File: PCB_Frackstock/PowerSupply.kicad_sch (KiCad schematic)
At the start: 25 parts, among them J2 105450-0101, U12 SPX3819M5-L-3-3, U13 SGM6603-5.0YN6G_TR, U14 1043, U3 MCP73871-2CC

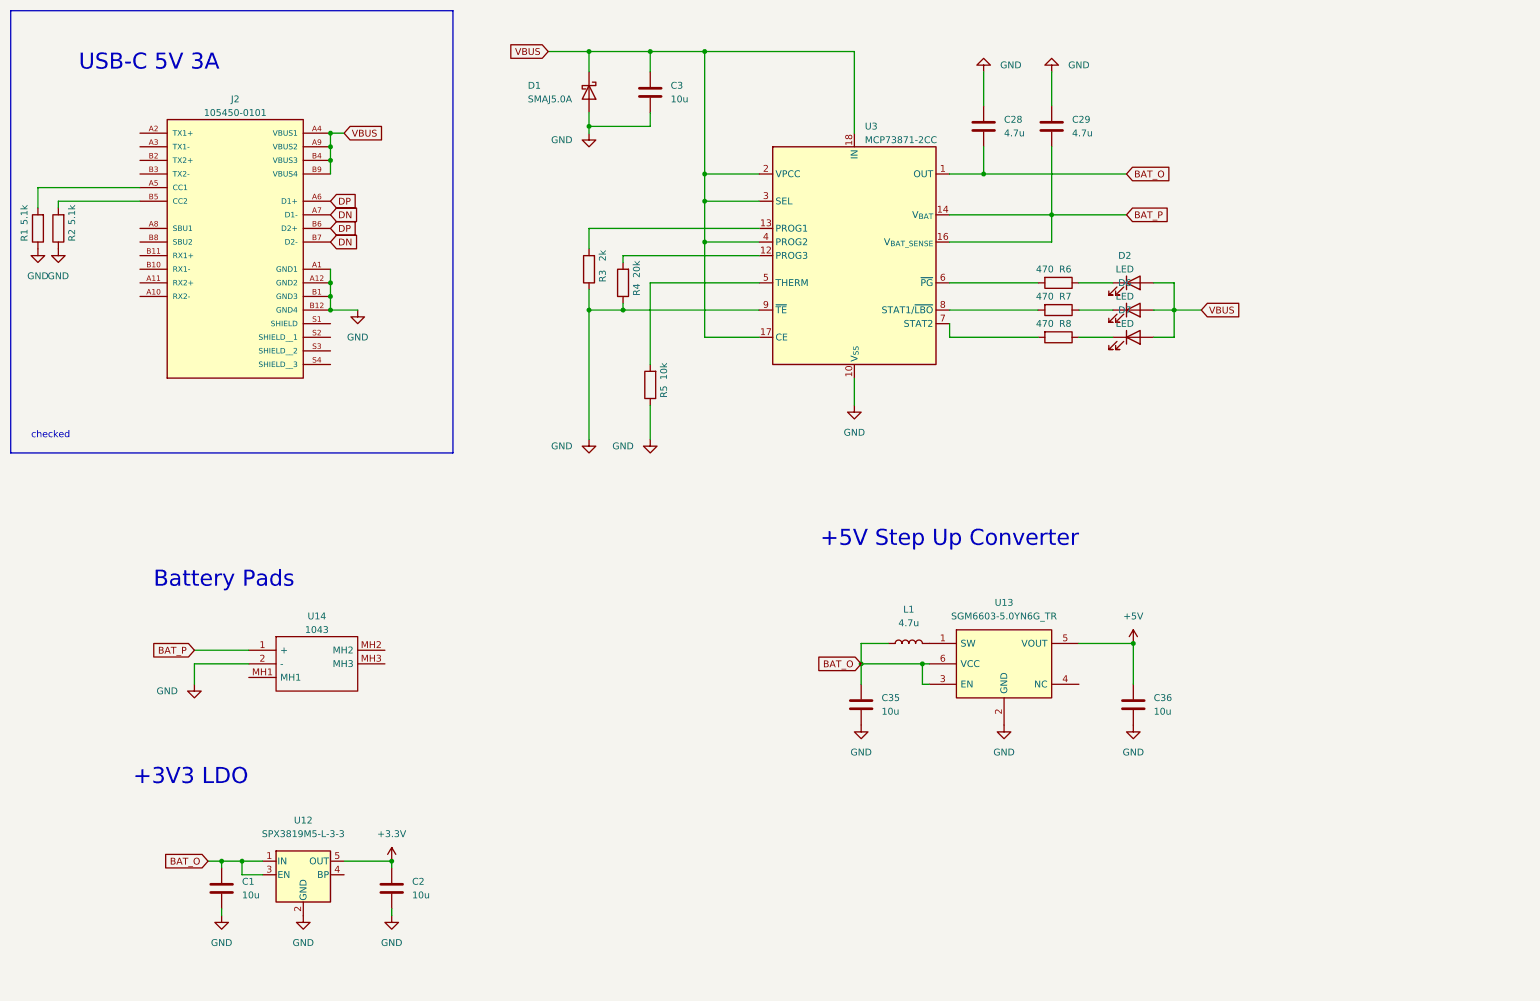
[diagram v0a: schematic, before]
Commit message: Battery Management and change parts to 0603
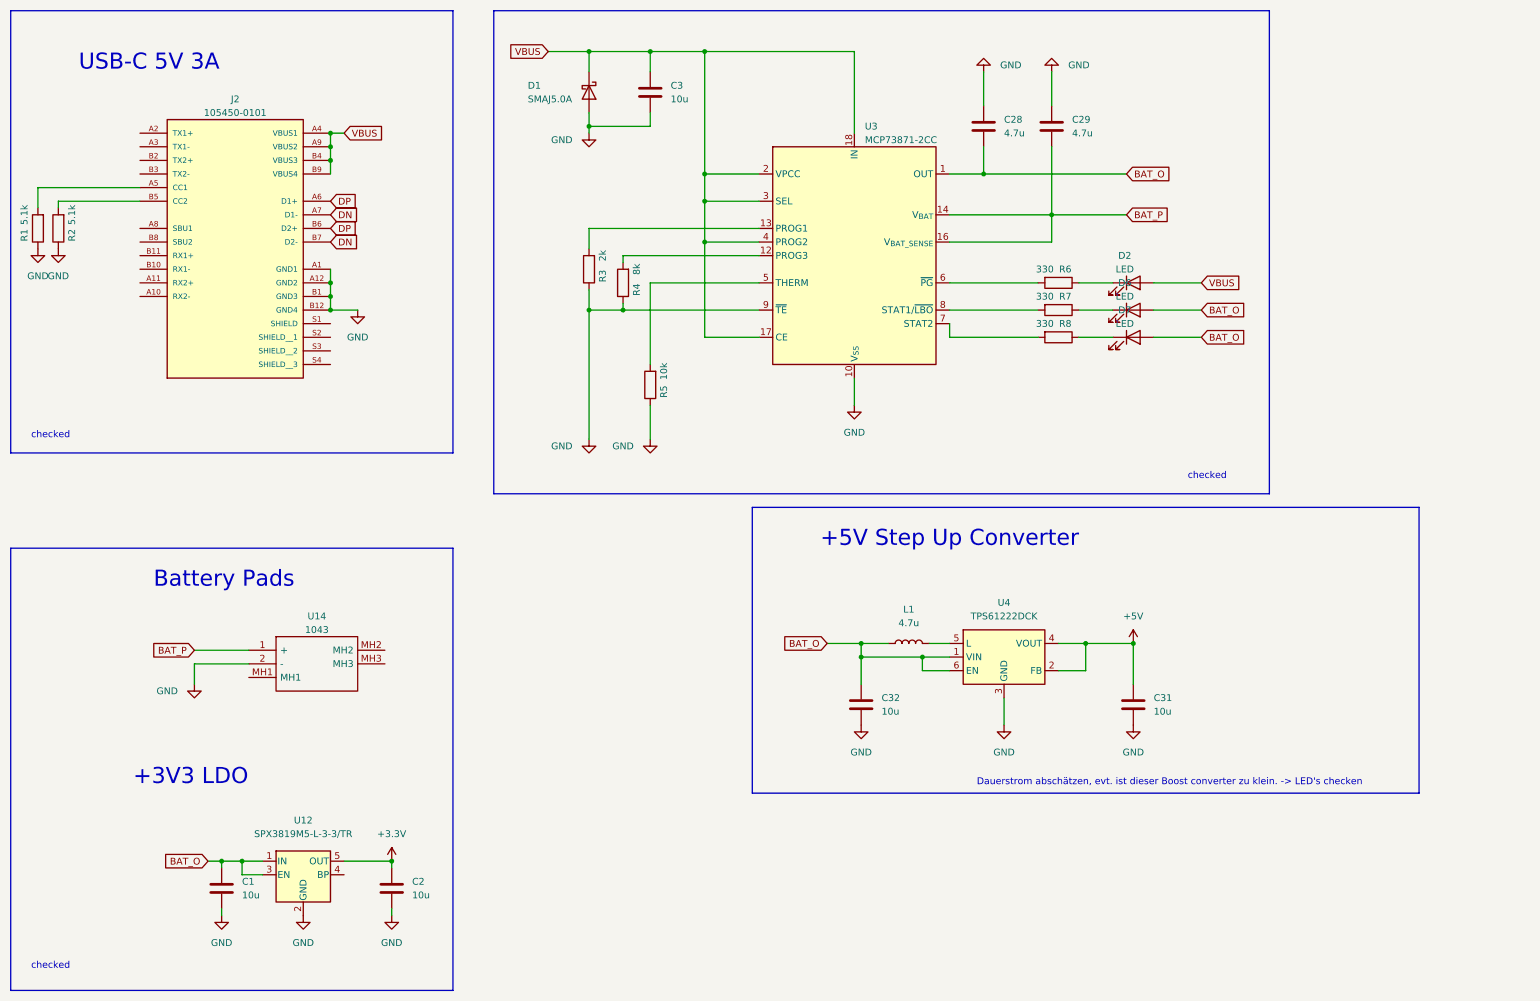
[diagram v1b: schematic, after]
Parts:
- removed C35, C36: 10u, Capacitor_SMD:C_0402_1005Metric, symbol Device:C
- removed U13: SGM6603-5.0YN6G_TR, SnapEDA Library:SOT23-6, symbol New_Library:SGM6603-5.0YN6G_TR
- added C31, C32: 10u, Capacitor_SMD:C_0603_1608Metric_Pad1.08x0.95mm_HandSolder, symbol Device:C
- added U4: TPS61222DCK, Package_TO_SOT_SMD:Texas_R-PDSO-G6, symbol Regulator_Switching:TPS61222DCK
- C1, C2: footprint Capacitor_SMD:C_0402_1005Metric -> Capacitor_SMD:C_0603_1608Metric_Pad1.08x0.95mm_HandSolder; LCSC C15525 -> (none); Note https://www.lcsc.com/product-detail/Multilayer-Ceramic-Capa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 -> (none); Vendor C1691 -> (none); vendor C1691 -> (none)
- D1: Info Aus Datenblatt MCP73871 (ESD und OV Schutz -> Aus Datenblatt MCP73871 (ESD und OV Schutz)
- D2: footprint (none) -> LED_SMD:LED_0603_1608Metric_Pad1.05x0.95mm_HandSolder; Info (none) -> Blue -> PG indicates Power from USB
- D6: footprint (none) -> LED_SMD:LED_0603_1608Metric_Pad1.05x0.95mm_HandSolder; Info (none) -> Red -> STAT1 indicates when Battery voltage is low
- D7: footprint (none) -> LED_SMD:LED_0603_1608Metric_Pad1.05x0.95mm_HandSolder; Info (none) -> Green -> Charge Complete, standby
- L1: LCSC C1034 -> (none); Note https://www.lcsc.com/product-detail/Inductors-SMD_Sunlord-S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 -> (none); Vendor C1034 -> (none); vendor C1034 -> (none)
- R4: value 20k -> 8k
- R6, R7, R8: value 470 -> 330
- U12: value SPX3819M5-L-3-3 -> SPX3819M5-L-3-3/TR; LCSC C9055 -> (none); Note https://www.lcsc.com/product-detail/Linear-Voltage-Regulato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 -> (none); Vendor C9055 -> (none); vendor C9055 -> (none)
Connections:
- net +5V: now also C31.1, U4.2 (FB), U4.4 (VOUT)
- net BAT_O: now also D6.2 (A), D7.2 (A), C32.1, U4.1 (VIN), U4.6 (EN)
- net GND: now also C31.2, C32.2, U4.3 (GND)
- net VBUS: no longer D6.2 (A), D7.2 (A)
- net at L1.2: now also U4.5 (L)
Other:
- note added: "Dauerstrom abschätzen, evt. ist dieser Boost converter zu klein. -> LED's checken"

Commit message: Schema fertig
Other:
- note added: "LED-Ring wird direkt mit der Batteriespannung gespiesen. Eine 5V Spannungsquelle wird somit garnicht gebraucht. (Wird drin gelassen falls doch)"
- note removed: "Dauerstrom abschätzen, evt. ist dieser Boost converter zu klein. -> LED's checken"
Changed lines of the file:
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@@
     (effects (font (size 1.27 1.27)) (justify left bottom))
   )
-  (text "Dauerstrom abschätzen, evt. ist dieser Boost converter zu klein. -> LED's checken"
-    (at 193.04 158.75 0)
+  (text "LED-Ring wird direkt mit der Batteriespannung gespiesen.\nEine 5V Spannungsquelle wird somit garnicht gebraucht.\n(Wird drin gelassen falls doch)\n"
+    (at 227.33 157.48 0)
     (effects (font (size 1.27 1.27)) (justify left bottom))
   )

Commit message: Schema_fertig
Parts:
- removed C1, C2, C31, C32: 10u, Capacitor_SMD:C_0603_1608Metric_Pad1.08x0.95mm_HandSolder, symbol Device:C
- removed L1: 4.7u, Inductor_SMD:L_0603_1608Metric, symbol Device:L
- removed U12: SPX3819M5-L-3-3/TR, Package_TO_SOT_SMD:SOT-23-5, symbol Regulator_Linear:SPX3819M5-L-3-3
- removed U4: TPS61222DCK, Package_TO_SOT_SMD:Texas_R-PDSO-G6, symbol Regulator_Switching:TPS61222DCK
- added TP1, TP2, TP3: TestPoint_Alt, TestPoint:TestPoint_Pad_1.5x1.5mm, symbol Connector:TestPoint_Alt
- U14: footprint KiCad:1043 -> Frack:Keystone_1043
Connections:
- net DN: now also TP1.1
- net DP: now also TP2.1
- net GND: now also J2.S1 (SHIELD), J2.S2 (SHIELD__1), J2.S3 (SHIELD__2), J2.S4 (SHIELD__3), TP3.1
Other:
- note removed: "+3V3 LDO"
- note removed: "+5V Step Up Converter"
- note removed: "LED-Ring wird direkt mit der Batteriespannung gespiesen. Eine 5V Spannungsquelle wird somit garnicht gebraucht. (Wird drin gelassen falls doch)"

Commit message: Layout Update
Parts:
- TP1, TP2: footprint TestPoint:TestPoint_Pad_1.5x1.5mm -> Frack:TestPoint_Pad_1.5x1.5mm_small
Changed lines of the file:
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@@
       (effects (font (size 1.27 1.27)) (justify left))
     )
-    (property "Footprint" "TestPoint:TestPoint_Pad_1.5x1.5mm" (at 45.72 144.78 0)
+    (property "Footprint" "Frack:TestPoint_Pad_1.5x1.5mm_small" (at 45.72 144.78 0)
       (effects (font (size 1.27 1.27)) hide)
     )
@@
   (symbol (lib_id "Connector:TestPoint_Alt") (at 40.64 165.1 0) (unit 1)
     (in_bom yes) (on_board yes) (dnp no) (fields_autoplaced)
-    (property "Reference" "TP3" (at 43.18 160.528 0)
-      (effects (font (size 1.27 1.27)) (justify left))
-    )
-    (property "Value" "TestPoint_Alt" (at 43.18 163.068 0)
+    (property "Reference" "TP3" (at 43.18 161.163 0)
+      (effects (font (size 1.27 1.27)) (justify left))
+    )
+    (property "Value" "TestPoint_Alt" (at 43.18 163.703 0)
       (effects (font (size 1.27 1.27)) (justify left))
     )
@@
       (effects (font (size 1.27 1.27)) (justify left))
     )
-    (property "Footprint" "TestPoint:TestPoint_Pad_1.5x1.5mm" (at 45.72 154.94 0)
-      (effects (font (size 1.27 1.27)) hide)
-    )
+    (property "Footprint" "Frack:TestPoint_Pad_1.5x1.5mm_small" (at 45.72 154.94 0)
+      (effects (font (size 1.27 1.27)) hide)
+    )

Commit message: Frackstock-Schema-review1.0
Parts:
- removed J2: 105450-0101, SnapEDA Library pretty:MOLEX_105450-0101, symbol 105450-0101:105450-0101
- removed R1, R2: 5.1k, Resistor_SMD:R_0603_1608Metric_Pad0.98x0.95mm_HandSolder, symbol Device:R
- removed TP1, TP2: TestPoint_Alt, Frack:TestPoint_Pad_1.5x1.5mm_small, symbol Connector:TestPoint_Alt
- removed TP3: TestPoint_Alt, TestPoint:TestPoint_Pad_1.5x1.5mm, symbol Connector:TestPoint_Alt
- added J5: VBUS, Connector_PinSocket_2.54mm:PinSocket_1x01_P2.54mm_Vertical, symbol Connector:Conn_01x01_Socket
- R4: value 8k -> 100k
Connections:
- net BAT_O: no longer D7.2 (A)
- net VBUS: now also D7.2 (A), J5.1 (Pin_1)
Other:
- note removed: "USB-C 5V 3A"
- note removed: "checked"
- moved on the sheet: C28, C29, C3, D1, D2, D6, D7, R3, R4, R5, R6, R7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

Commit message: Schema-review-1
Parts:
- removed C28, C29: 4.7u, Capacitor_SMD:C_0603_1608Metric_Pad1.08x0.95mm_HandSolder, symbol Device:C
- added C1, C2: 4.7u, Capacitor_SMD:C_0603_1608Metric_Pad1.08x0.95mm_HandSolder, symbol Device:C
- D2: value LED -> Blau
- D6: value LED -> Rot
- D7: value LED -> Grün
- R4: value 100k -> 8.2k
- R6, R8: value 330 -> 390
- R7: value 330 -> 430
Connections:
- net BAT_O: now also C2.1
- net BAT_P: now also C1.1
- net GND: now also C1.2, C2.2
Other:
- company: (none) -> Eberkreis
- title: (none) -> Frackstock ET2024
- moved on the sheet: D2, D6, D7, R6, R7, R8

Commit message: Fracstock PCB final commit
DRC check, PCB review done, ready to order
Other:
- company: Eberkreis -> Eberkreis Engineering
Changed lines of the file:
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@@
     (date "2024-03-24")
     (rev "2")
-    (company "Eberkreis")
+    (company "Eberkreis Engineering")
   )
   (junction (at 44.45 49.53) (diameter 0) (color 0 0 0 0)
